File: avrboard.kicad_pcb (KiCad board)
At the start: 2 copper layers, 20 parts, among them IC1 ATMEGA328P-P, P1 FTDI, P2 ICSP, SW1 RESET, U1 7805, X1 16MHz

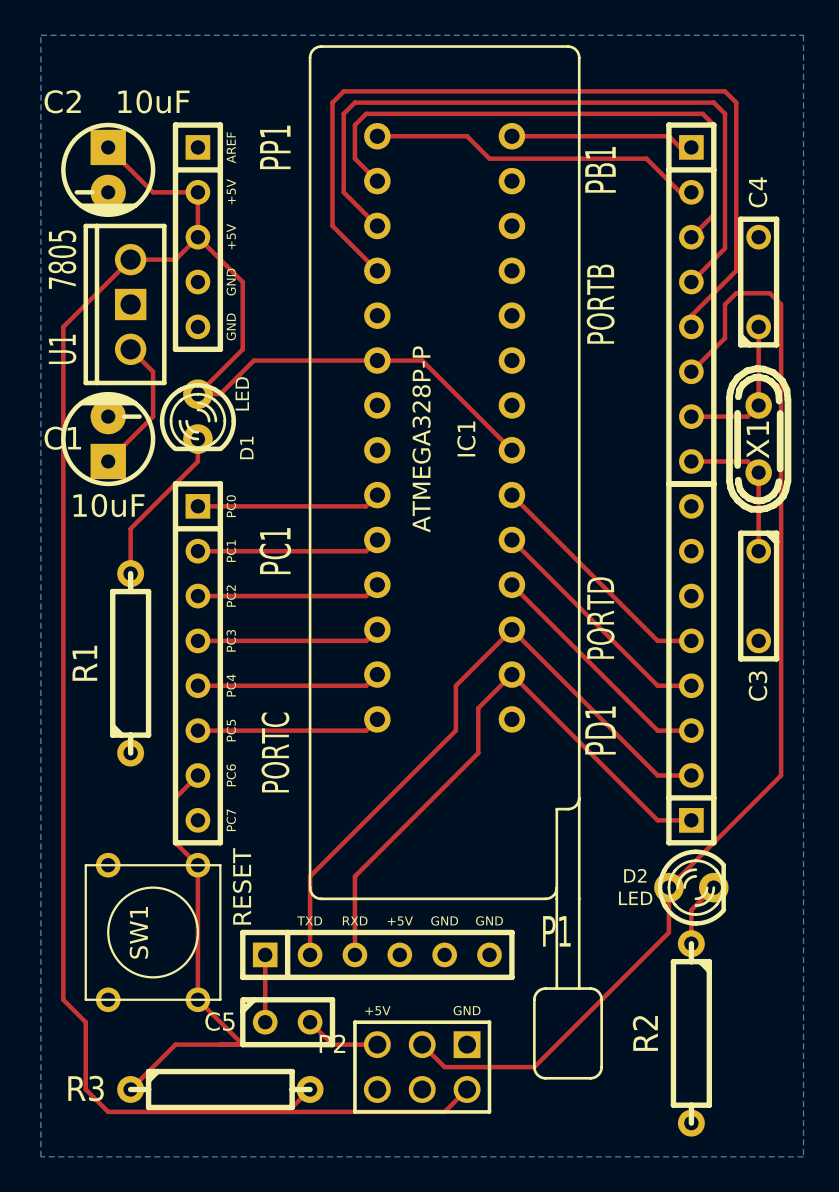
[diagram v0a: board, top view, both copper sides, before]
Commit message: Route to the the RESET pin via the back of the board.
This allows the RESET signal to hope over the serial TX/RX signals.
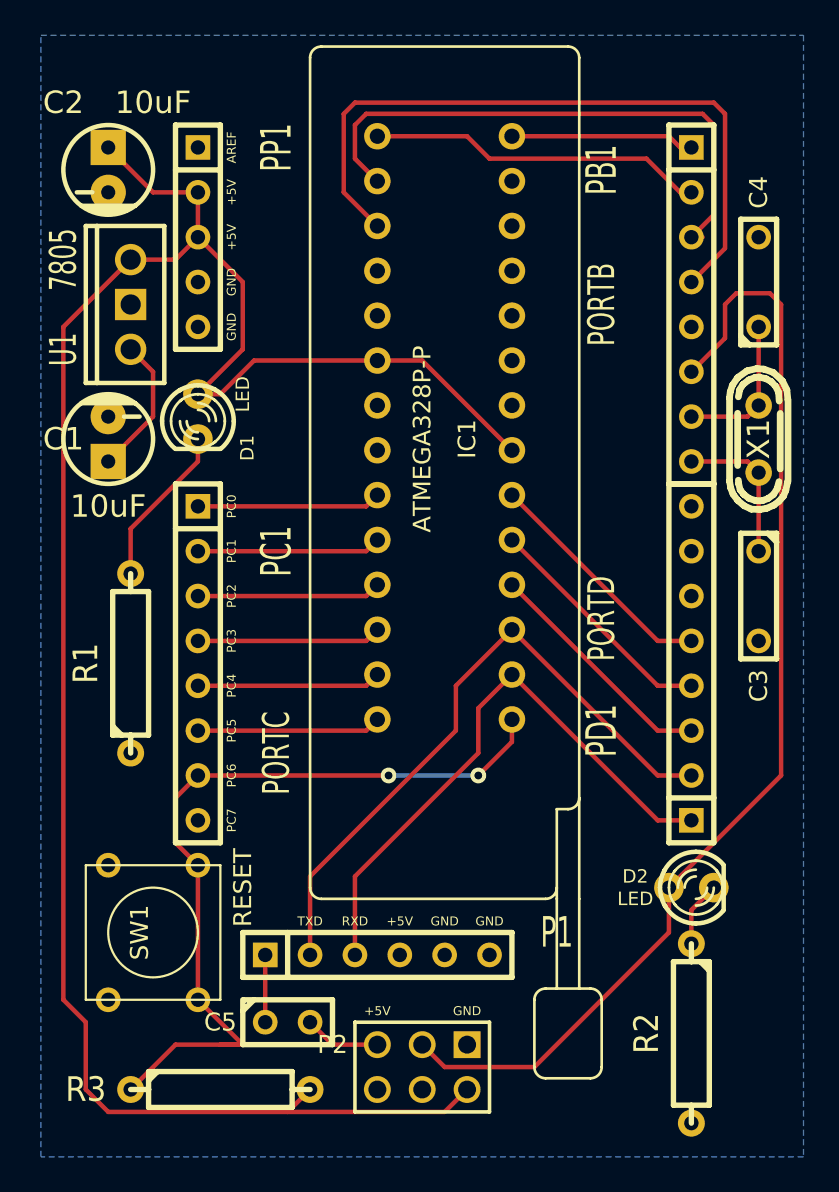
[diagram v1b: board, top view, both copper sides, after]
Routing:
- net /PB4: track 47.7 -> 0.00 mm
- net /RESET: track 35.4 -> 55.3 mm, vias 0 -> 2
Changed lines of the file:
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@@
     (thickness 1.6)
     (drawings 20)
-    (tracks 120)
+    (tracks 118)
     (zones 0)
     (modules 20)
@@
   (segment (start 162.56 45.72) (end 162.56 40.64) (width 0.254) (layer F.Cu) (net 5))
   (segment (start 161.29 46.99) (end 161.925 46.99) (width 0.254) (layer F.Cu) (net 5))
-  (segment (start 161.29 49.53) (end 163.195 47.625) (width 0.254) (layer F.Cu) (net 6) (status 400000))
-  (segment (start 141.605 44.45) (end 143.51 46.355) (width 0.254) (layer F.Cu) (net 6) (status 800000))
+  (segment (start 161.29 49.53) (end 163.195 47.625) (width 0.254) (layer F.Cu) (net 6))
+  (segment (start 141.605 44.45) (end 143.51 46.355) (width 0.254) (layer F.Cu) (net 6))
   (segment (start 141.605 40.005) (end 141.605 44.45) (width 0.254) (layer F.Cu) (net 6))
   (segment (start 142.24 39.37) (end 141.605 40.005) (width 0.254) (layer F.Cu) (net 6))
@@
   (segment (start 163.195 40.005) (end 162.56 39.37) (width 0.254) (layer F.Cu) (net 6))
   (segment (start 163.195 47.625) (end 163.195 40.005) (width 0.254) (layer F.Cu) (net 6))
-  (segment (start 161.29 52.07) (end 161.29 51.435) (width 0.254) (layer F.Cu) (net 7) (status C00000))
-  (segment (start 161.29 51.435) (end 163.83 48.895) (width 0.254) (layer F.Cu) (net 7) (status 400000))
-  (segment (start 163.83 48.895) (end 163.83 39.37) (width 0.254) (layer F.Cu) (net 7))
-  (segment (start 163.83 39.37) (end 163.195 38.735) (width 0.254) (layer F.Cu) (net 7))
-  (segment (start 163.195 38.735) (end 141.605 38.735) (width 0.254) (layer F.Cu) (net 7))
-  (segment (start 141.605 38.735) (end 140.97 39.37) (width 0.254) (layer F.Cu) (net 7))
-  (segment (start 140.97 39.37) (end 140.97 46.355) (width 0.254) (layer F.Cu) (net 7))
-  (segment (start 140.97 46.355) (end 143.51 48.895) (width 0.254) (layer F.Cu) (net 7) (status 800000))
   (segment (start 160.02 83.82) (end 166.37 77.47) (width 0.254) (layer F.Cu) (net 8))
   (segment (start 163.195 52.705) (end 161.29 54.61) (width 0.254) (layer F.Cu) (net 8))
@@
   (segment (start 161.29 69.85) (end 159.385 69.85) (width 0.254) (layer F.Cu) (net 20))
   (segment (start 159.385 69.85) (end 151.13 61.595) (width 0.254) (layer F.Cu) (net 20))
+  (segment (start 133.35 77.47) (end 144.145 77.47) (width 0.254) (layer F.Cu) (net 24) (status 400000))
+  (segment (start 151.13 75.565) (end 151.13 74.295) (width 0.254) (layer F.Cu) (net 24) (status 800000))
+  (segment (start 149.225 77.47) (end 151.13 75.565) (width 0.254) (layer F.Cu) (net 24))
+  (via (at 149.225 77.47) (size 0.889) (layers F.Cu B.Cu) (net 24))
+  (segment (start 144.145 77.47) (end 149.225 77.47) (width 0.254) (layer B.Cu) (net 24))
+  (via (at 144.145 77.47) (size 0.889) (layers F.Cu B.Cu) (net 24))
   (segment (start 133.35 82.55) (end 132.08 81.28) (width 0.254) (layer F.Cu) (net 24))
   (segment (start 132.08 78.74) (end 133.35 77.47) (width 0.254) (layer F.Cu) (net 24))
